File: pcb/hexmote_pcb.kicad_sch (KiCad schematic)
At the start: 23 parts, among them J1 ICM-20948, SW1 SW_Push_45deg, SW10 SW_SPDT, SW2 SW_Push_45deg, SW3 SW_Push_45deg, SW4 SW_Push_45deg, SW5 SW_Push_45deg, SW6 SW_Push_45deg, SW7 SW_Push_45deg, SW8 SW_Push_45deg, SW9 SW_Push_45deg, U1 SuperMini nRF52840, U2 Joystick

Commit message: fixed joystick button having extra button
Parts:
- removed SW9: SW_Push_45deg, symbol Switch:SW_Push_45deg
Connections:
- net COL3: now also U2.B1A (SEL+)
- net GND: no longer U2.B2A (SEL-)
- net SEL-: now reaches D9.2 (A)
- net SEL-: now also U2.B2A (SEL-)
- net SEL: no longer names the net of U1.17 (P0.31-LF)
- net SEL: no longer U2.B1A (SEL+)

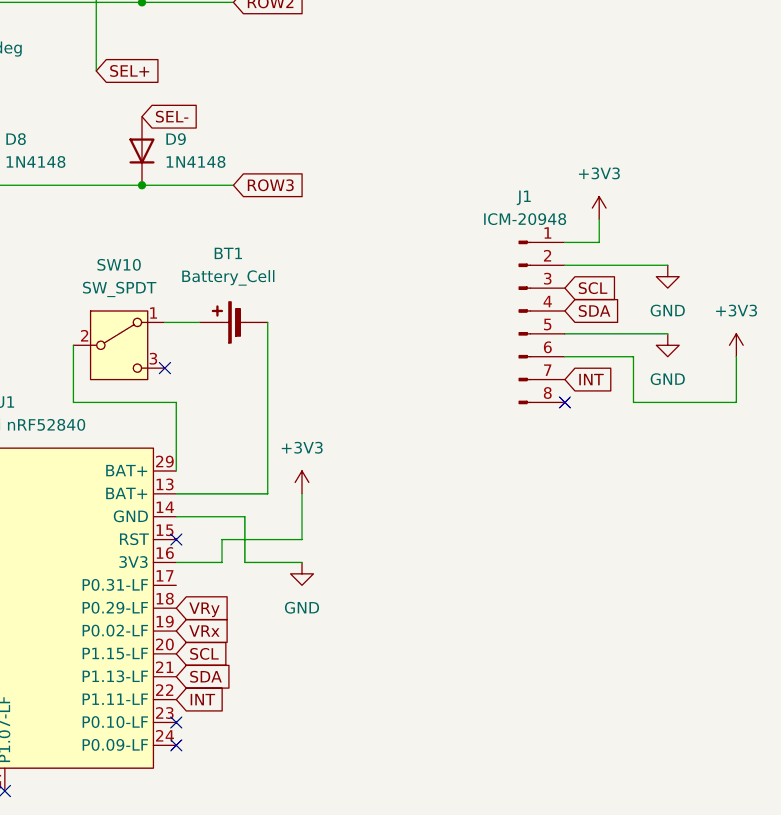
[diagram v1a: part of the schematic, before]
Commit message: finished schematic and layed out components
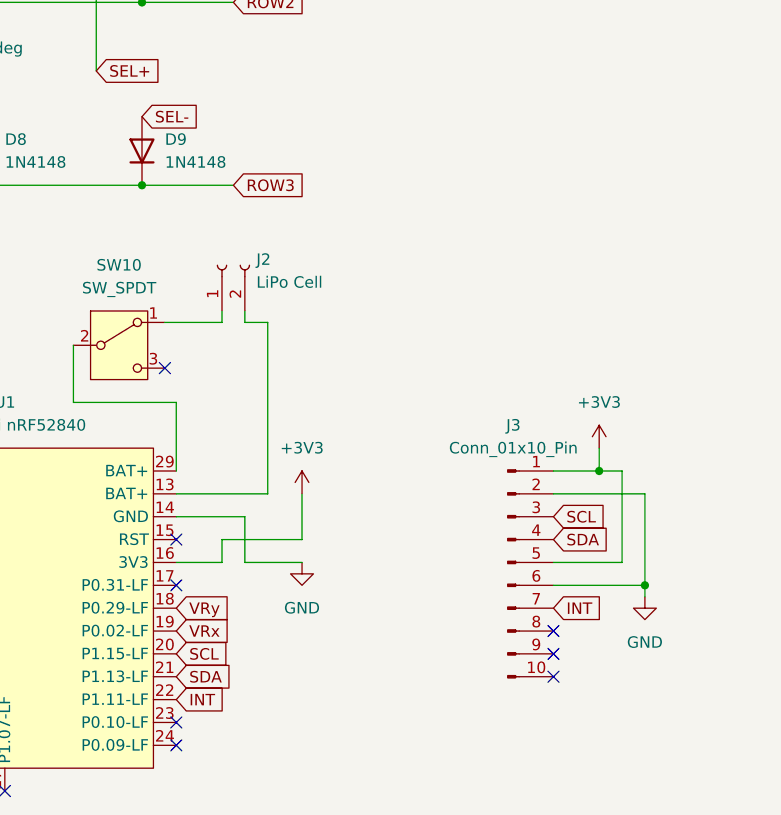
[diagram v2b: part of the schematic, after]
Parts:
- removed BT1: Battery_Cell, symbol Device:Battery_Cell
- removed J1: ICM-20948, symbol Connector:Conn_01x08_Pin
- added J2: LiPo Cell, Connector_JST:JST_PH_S2B-PH-K_1x02_P2.00mm_Horizontal, symbol Connector:Conn_01x02_Socket
- added J3: Conn_01x10_Pin, extra_footprints:ICM-20498_Board, symbol Connector:Conn_01x10_Pin
- D1, D2, D3, D4, D5, D6, D7, D8, D9: footprint Diode_SMD:D_SOD-523 -> Diode_THT:D_DO-35_SOD27_P7.62mm_Horizontal
- SW1, SW2, SW3, SW4, SW5, SW6: footprint (none) -> buttons:Soft_Tactile_Button_6.00x4.5mm
- SW10: footprint (none) -> Button_Switch_THT:SW_Slide_SPDT_Straight_CK_OS102011MS2Q
- SW7, SW8: footprint (none) -> Button_Switch_THT:SW_Tactile_SPST_Angled_PTS645Vx58-2LFS
- U1: footprint Package_DFN_QFN:Nordic_AQFN-73-1EP_7x7mm_P0.5mm -> extra_footprints:SuperMini NRF52840
- U2: footprint XDCR_COM-09032 -> PS4_joystick_footprint-main:PS4_joystick
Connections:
- net +3V3: now also J3.1 (Pin_1), J3.5 (Pin_5)
- net GND: now also J3.2 (Pin_2), J3.6 (Pin_6)
- net INT: now also J3.7 (Pin_7)
- net SCL: now also J3.3 (Pin_3)
- net SDA: now also J3.4 (Pin_4)
- net at U1.13 (BAT+): now also J2.2 (Pin_2)
- net at SW10.1 (A): now also J2.1 (Pin_1)
- no-connect marks 12 -> 15

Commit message: finished PCB
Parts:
- removed D1, D2, D3, D4, D5, D6, D7, D8, D9: 1N4148, Diode_THT:D_DO-35_SOD27_P7.62mm_Horizontal, symbol Diode:1N4148
- removed SW1, SW2, SW3, SW4, SW5, SW6: SW_Push_45deg, buttons:Soft_Tactile_Button_6.00x4.5mm, symbol Switch:SW_Push_45deg
- removed SW7, SW8: SW_Push_45deg, Button_Switch_THT:SW_Tactile_SPST_Angled_PTS645Vx58-2LFS, symbol Switch:SW_Push_45deg
- added H1, H2, H3, H4: MountingHole, MountingHole:MountingHole_3.2mm_M3, symbol Mechanical:MountingHole
- added SW1, SW2, SW3, SW4, SW5, SW6: SW_Push, buttons:Soft_Tactile_Button_6.00x4.5mm, symbol Switch:SW_Push
- added SW7, SW8: SW_Push, Button_Switch_THT:SW_Tactile_SPST_Angled_PTS645Vx58-2LFS, symbol Switch:SW_Push
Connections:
- net +3.3V is gone; now on net +3V3: U2.H1 (H+), U2.V1 (V+)
- net SEL- is gone; now on net GND: U2.B2A (SEL-)
- net GND: now also SW1.2, SW2.2, SW3.2, SW4.2, SW5.2, SW6.2, SW7.2, SW8.2
- net INT: now also U1.12 (P1.06-LF); no longer U1.22 (P1.11-LF)
- net SCL: now also U1.10 (P0.11); no longer U1.20 (P1.15-LF)
- net SDA: now also U1.11 (P1.04-LF); no longer U1.21 (P1.13-LF)
- net VRx: now also U1.17 (P0.31-LF); no longer U1.19 (P0.02-LF)
- net VRy: now also U1.19 (P0.02-LF); no longer U1.18 (P0.29-LF)
- net L: now reaches U1.1 (P0.06)
- net L: now also SW7.1
- net -: now reaches U1.2 (P0.08)
- net -: now also SW6.1
- net A: now reaches U1.24 (P0.09-LF)
- net A: now also SW1.1
- net COL1: no longer names the net of U1.8 (P0.24)
- net COL2 renamed SEL
- net SEL: now also U2.B1A (SEL+)
- removed net COL3: U1.10 (P0.11), U2.B1A (SEL+)
- net ROW1 renamed R
- net R: now also SW8.1
- net ROW2 renamed +
- net +: now also SW5.1
- net ROW3: no longer names the net of U1.7 (P0.22)
- new net B: SW2.1, U1.22 (P1.11-LF)
- new net X: SW3.1, U1.21 (P1.13-LF)
- new net Y: SW4.1, U1.20 (P1.15-LF)
- no-connect marks 15 -> 8
